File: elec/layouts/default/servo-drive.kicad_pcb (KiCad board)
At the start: 4 copper layers, 37.5 x 39 mm, 137 parts, among them U2 8Mhz

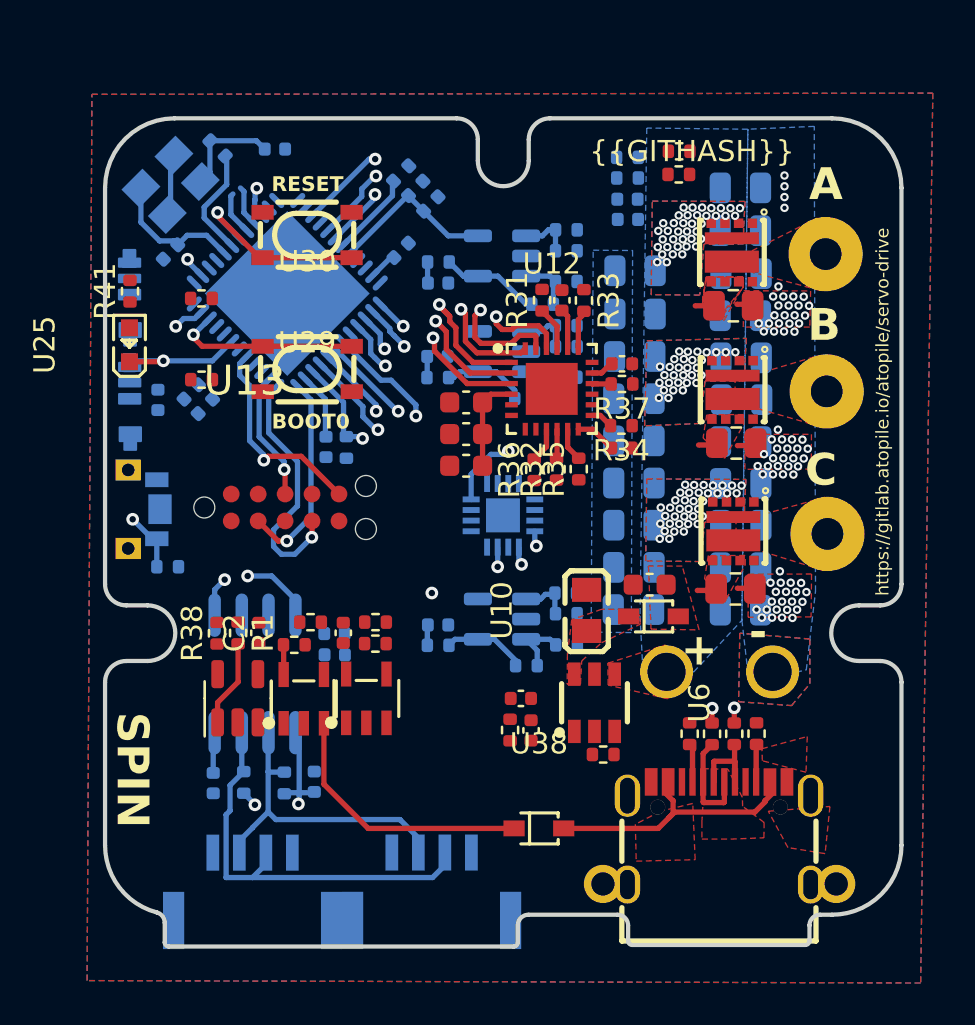
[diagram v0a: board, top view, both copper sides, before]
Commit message: big ol refactor, added lots of interfaces, changed pinout to match moteus controller, layout changed to add more connectors
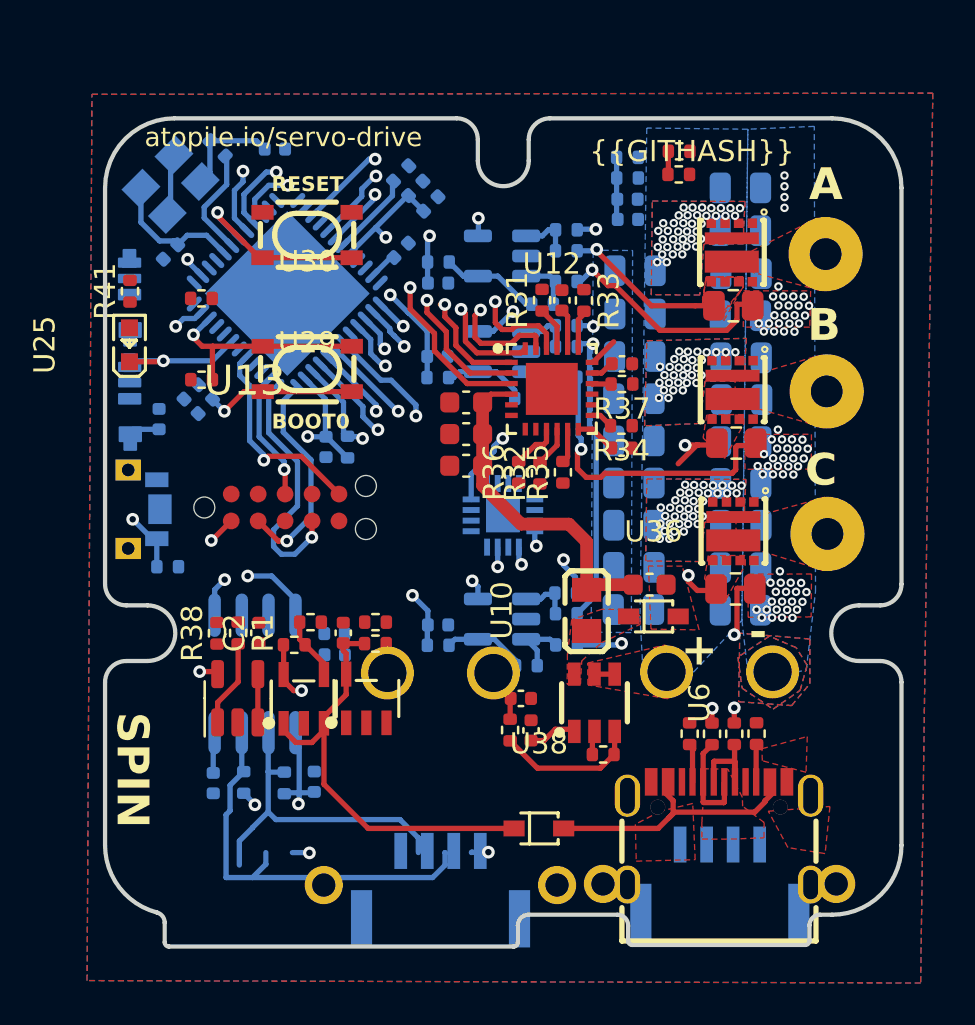
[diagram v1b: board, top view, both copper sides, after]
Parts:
- added U14: , lib:CONN-TH_XT30PW-M, B.Cu at (220.8, 112.8)
- moved U27 13.6 mm to (233.9, 118.0)
- moved U26 8.86 mm to (220.8, 118.3)
- moved C18 0.91 mm to (207.5, 95.8), turned to 90 degrees
- moved R32 0.80 mm to (225.5, 98.4)
- moved R35 0.76 mm to (226.5, 98.3)
- moved R36 0.74 mm to (224.5, 98.3)
- moved R15 0.06 mm to (216.4, 97.1)
- renumbered C44 to C42, C42 to C44
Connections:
- net SpinServoNEMA17-cs renamed SpinServoNEMA17-spi_cs
- net SpinServoNEMA17-enum_sw renamed SpinServoNEMA17-in
- net SpinServoNEMA17-mosi renamed SpinServoNEMA17-spi_mosi
- net SpinServoNEMA17-sck renamed SpinServoNEMA17-spi_sck
- net _a-high_gate-1 renamed _a-high_gate-2
- net _a-low_gate-1 renamed _a-low_gate-2
- net _b-high_gate-1 renamed _b-high_gate-2
- net _b-i_in renamed _b-gnd-1
- net _b-low_gate-1 renamed _b-low_gate-2
- net _c-gnd renamed _c-gnd-1
- net _c-high_gate-1 renamed _c-high_gate-2
- net _c-low_gate-1 renamed _c-low_gate-2
- net _hb-vcc_pwr renamed _hb-vcc_pwr-7
- net _hb-vcc_pwr-1 renamed _hb-vcc_pwr-9
- net _hb-vcc_pwr-2 renamed _hb-vcc_pwr-8
- net _i_sense-in-3 renamed _i_sense-in-5
- net _i_sense-in_n-3 renamed _i_sense-in_n-5
- net _i_sense-in_p-1 renamed _i_sense-output-9
- net _i_sense-in_p-2 renamed _i_sense-output-8
- net _i_sense-input-6 renamed _i_sense-p1-8
- net _i_sense-out-1 renamed _i_sense-in-6
- net _i_sense-output-4 renamed _i_sense-output-7
- net _i_sense-output-5 renamed _i_sense-in_n-6
- net _i_sense-p1-3 renamed _i_sense-p1-7
- net _i_sense-p1-4 renamed _i_sense-input-10
- net _i_sense-p1-5 renamed _i_sense-input-8
- net drv8300-EP-1 renamed drv8300-EP-2
- net drv8300-MODE-1 renamed drv8300-MODE-2
- net drv8300-NC1-1 renamed drv8300-NC1-2
- net drv8300-NC2-1 renamed drv8300-NC2-2
- net gate_reg-sw-1 renamed gate_reg-sw
- net micro_kit-in-1 renamed micro_kit-PB8_BOOT0
- net power_stage-DT renamed power_stage-DT-1
- net power_stage-GHA renamed power_stage-GHA-1
- net power_stage-GHB renamed power_stage-GHB-1
- net power_stage-GHC renamed power_stage-GHC-1
- net power_stage-GLA renamed power_stage-GLA-1
- net power_stage-GLB renamed power_stage-GLB-1
- net power_stage-GLC renamed power_stage-GLC-1
- net power_stage-bs renamed power_stage-bs-3
- net power_stage-bs-1 renamed power_stage-BSTC-1
- net power_stage-i_fb_zero renamed power_stage-i_fb_zero-1
- net vref_1V65-vref_unbuf-1 renamed vref_1V65-vref_unbuf-2
- C10 pad 1: _a-out -> SpinServoNEMA17-a_isense
- C11 pad 1: _b-out-1 -> SpinServoNEMA17-b_isense
- C12 pad 1: _c-i_fb -> SpinServoNEMA17-c_isense
- C14 pad 1: micro_kit-in-3 -> micro_kit-in-4
- R11 pad 2: micro_kit-in-2 -> micro_kit-in-3
- R13 pad 1: _i_sense-p1-2 -> _i_sense-input-7
- R16 pad 2: _a-out -> SpinServoNEMA17-a_isense
- R46 pad 2: _b-out-1 -> SpinServoNEMA17-b_isense
- R50 pad 1: _i_sense-input-7 -> _i_sense-input-9
- R52 pad 2: _c-i_fb -> SpinServoNEMA17-c_isense
- U15 pad 5: micro_kit-in-3 -> micro_kit-in-4
- U15 pad 7: micro_kit-in-2 -> micro_kit-in-3
- U17 pad 1: _i_sense-p1-2 -> _i_sense-input-7
- U2 pad 1: micro_kit-in-3 -> micro_kit-in-4
- U29 pad 1: micro_kit-in-2 -> micro_kit-in-3
- U29 pad 2: micro_kit-in-2 -> micro_kit-in-3
- U34 pad 1: _i_sense-input-7 -> _i_sense-input-9
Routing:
- net power_stage-i_fb_zero-1: track 0.00 -> 23.7 mm, vias 0 -> 2
- net SpinServoNEMA17-v_3: track 13.8 -> 30.0 mm, vias 0 -> 11
- net SpinServoNEMA17-a_isense: track 2.07 -> 17.7 mm, vias 0 -> 2
- net SpinServoNEMA17-b_isense: track 1.92 -> 17.0 mm, vias 0 -> 2
- net _i_sense-p1-8: track 0.00 -> 13.4 mm, vias 0 -> 1
- net SpinServoNEMA17-v_gate: track 4.51 -> 17.0 mm
- net _i_sense-input-8: track 0.00 -> 10.4 mm, vias 0 -> 2
- net _i_sense-input-10: track 0.00 -> 10.2 mm, vias 0 -> 2
- net _i_sense-p1-7: track 0.00 -> 9.89 mm, vias 0 -> 1
- net SpinServoNEMA17-v_5: track 12.7 -> 22.5 mm
- net micro_kit-in-2: track 8.93 -> 0.00 mm, vias 1 -> 0
- net _i_sense-input-9: track 0.00 -> 8.91 mm, vias 0 -> 2
- net gate_reg-fb-1: track 0.00 -> 6.80 mm
- net _i_sense-input-7: track 0.00 -> 6.75 mm, vias 0 -> 1
- net micro_kit-in-4: track 0.00 -> 6.51 mm
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- added copper zone on In2.Cu, net ldo_3v3-output
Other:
- board text added: "atopile.io/servo-drive"
- board text removed: "https://gitlab.atopile.io/atopile/servo-drive"

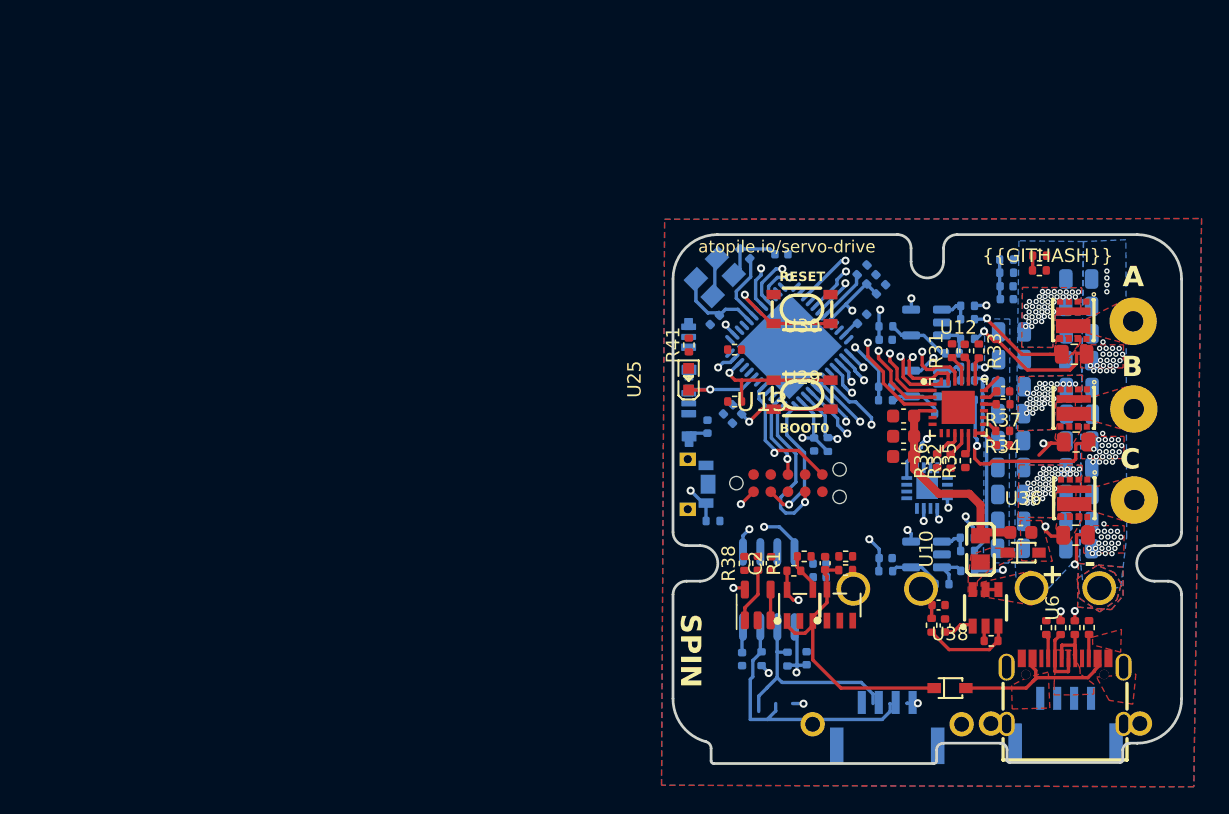
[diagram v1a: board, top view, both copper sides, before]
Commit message: Modified micro pinout to match moteus, because they are pretty sick, updated modules to use interfaces where posible, generated netlist and imported to Kicad project
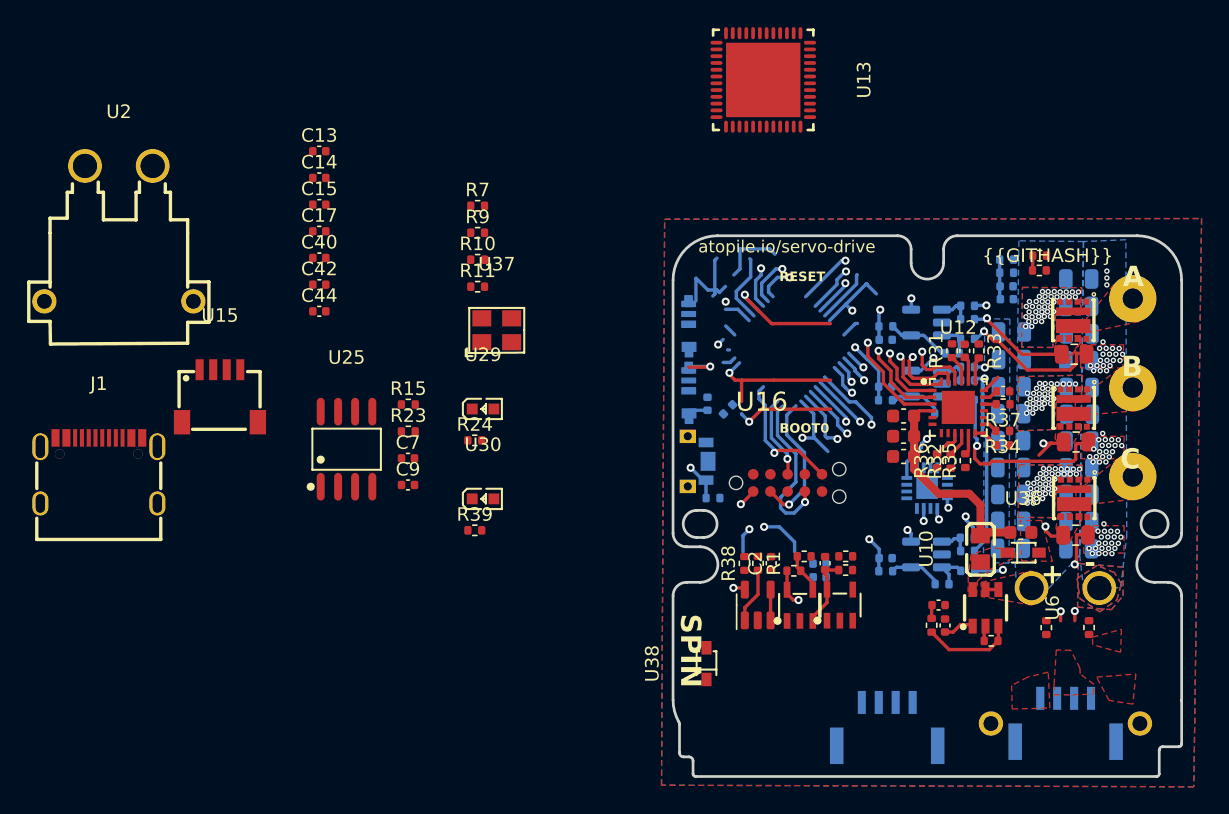
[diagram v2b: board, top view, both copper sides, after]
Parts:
- removed the C3 at (218.9, 87.9)
- removed the C4 at (219.6, 84.9)
- removed the C6 at (209.7, 95.2)
- removed R40: 60R, Resistor_SMD:R_0402_1005Metric
- removed R41: 1k, Resistor_SMD:R_0402_1005Metric
- removed the U14 at (220.8, 112.8)
- added C40: 1uF, Capacitor_SMD:C_0402_1005Metric, F.Cu at (178.8, 83.4)
- added C42: 20pF, Capacitor_SMD:C_0402_1005Metric, F.Cu at (178.8, 85.3)
- added C44: 20pF, Capacitor_SMD:C_0402_1005Metric, F.Cu at (178.8, 87.3)
- added U37: 8Mhz, lib:OSC-SMD_4P-L3.2-W2.5-BL, F.Cu at (191.9, 88.7)
- C13, C7, R7: moved to F.Cu
- C14, C15: value 20pF -> 100nF; moved to F.Cu
- C17: value 10nF -> 100nF; moved to F.Cu
- C9: value 1uF -> 10nF; moved to F.Cu
- R11: value 10k -> 1k5
- R15: value 1k5 -> 60R; moved to F.Cu
- R23: value 100k -> 60R
- R24: value 100k -> 1k; moved to F.Cu
- R39: value 60R -> 1k; moved to F.Cu
- U13: footprint lib:TAG-CONNECT_TC2050-IDC -> lib:UFQFPN-48_L7.0-W7.0-P0.50-BL-EP
- U15: footprint lib:UFQFPN-48_L7.0-W7.0-P0.50-BL-EP -> lib:CONN-SMD_4P-P1.00_SM04B-SRSS-TB-LF-SN; moved to F.Cu
- U16: footprint lib:SOIC-8_L4.9-W3.9-P1.27-LS6.0-BL -> lib:TAG-CONNECT_TC2050-IDC; moved to F.Cu
- U2: value 8Mhz -> (none); footprint lib:OSC-SMD_4P-L3.2-W2.5-BL -> lib:CONN-TH_XT30PW-M; moved to F.Cu
- U25: footprint lib:LED0603-RD -> lib:SOIC-8_L4.9-W3.9-P1.27-LS6.0-BL
- U29, U30: footprint lib:KEY-SMD_4P-L4.2-W3.2-P2.20-LS4.6 -> lib:LED0603-RD
- moved J1 73.2 mm to (162.6, 99.1)
- moved R9 52.9 mm to (190.5, 81.5), turned to 0 degrees
- moved R10 50.9 mm to (190.5, 83.5), turned to 0 degrees
- moved C13 48.8 mm to (178.8, 75.5), turned to 0 degrees
- moved C17 47.8 mm to (178.8, 81.4), turned to 0 degrees
- moved U2 44.1 mm to (164.0, 81.6), turned to 0 degrees
- moved U15 42.2 mm to (171.5, 93.5), turned to 0 degrees
- moved C7 37.1 mm to (185.4, 98.1), turned to 0 degrees
- moved C15 34.3 mm to (178.8, 79.4)
- moved R24 31.2 mm to (190.3, 96.8), turned to 0 degrees
- moved R15 31.1 mm to (185.4, 94.2), turned to 0 degrees
- moved C14 31.0 mm to (178.8, 77.4), turned to 0 degrees
- moved C9 30.1 mm to (185.4, 100.1), turned to 0 degrees
- moved U13 29.8 mm to (211.6, 70.2), turned to -90 degrees
- moved U25 25.8 mm to (180.8, 97.5), turned to 0 degrees
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- renumbered C40 to C3, C44 to C4, C42 to C6
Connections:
- net SpinServoNEMA17-anode renamed SpinServoNEMA17-vbus
- net SpinServoNEMA17-data_in renamed SpinServoNEMA17-data_out
- net _a-gnd-1 renamed _a-i_in-1
- net _b-gnd-1 renamed _b-i_in-1
- net _c-gnd-1 renamed _c-i_in-1
- net _i_sense-in-5 renamed _i_sense-out-4
- net _i_sense-in_n-5 renamed _i_sense-in_n-7
- net _i_sense-input-8 renamed _i_sense-input-11
- net _i_sense-output-8 renamed _i_sense-in_p-1
- net _i_sense-output-9 renamed _i_sense-in_p-2
- net _i_sense-p1-8 renamed _i_sense-input-12
- net gate_reg-sw renamed gate_reg-sw-1
- net ldo_3v3-output renamed ldo_3v3-adj-1
- net usb-sbu-1 renamed usbc-sbu-1
- C1 pad 1: SpinServoNEMA17-v_3 -> SpinServoNEMA17-vcc
- C13 pad 1: SpinServoNEMA17-v_3 -> SpinServoNEMA17-vcc
- C14 pad 1: micro_kit-in-4 -> SpinServoNEMA17-vcc
- C15 pad 1: micro_kit-out-1 -> SpinServoNEMA17-vcc
- C16 pad 1: SpinServoNEMA17-v_5 -> SpinServoNEMA17-gnd
- C17 pad 1: canbus-v_mid-2 -> SpinServoNEMA17-vcc
- C18 pad 1: SpinServoNEMA17-v_5 -> SpinServoNEMA17-gnd
- C19 pad 1: SpinServoNEMA17-v_3 -> SpinServoNEMA17-vcc
- C20 pad 1: SpinServoNEMA17-v_pwr -> power_stage-vcc_pwr-1
- C21 pad 1: SpinServoNEMA17-v_pwr -> power_stage-vcc_pwr-1
- C22 pad 1: SpinServoNEMA17-v_pwr -> power_stage-vcc_pwr-1
- C23 pad 1: SpinServoNEMA17-v_gate -> SpinServoNEMA17-gnd
- C25 pad 1: SpinServoNEMA17-v_pwr -> power_stage-vcc_pwr-1
- C26 pad 1: SpinServoNEMA17-v_pwr -> power_stage-vcc_pwr-1
- C27 pad 1: SpinServoNEMA17-v_pwr -> power_stage-vcc_pwr-1
- C28 pad 1: SpinServoNEMA17-v_pwr -> SpinServoNEMA17-vcc-1
- C29 pad 1: SpinServoNEMA17-v_pwr -> power_stage-vcc_pwr-1
- C3 pad 1: SpinServoNEMA17-v_pwr -> power_stage-vcc_pwr-1
- C30 pad 1: SpinServoNEMA17-v_pwr -> power_stage-vcc_pwr-1
- C31 pad 1: SpinServoNEMA17-v_gate -> SpinServoNEMA17-gnd
- C32 pad 1: SpinServoNEMA17-v_gate -> SpinServoNEMA17-gnd
- C33 pad 1: SpinServoNEMA17-out -> SpinServoNEMA17-vin_sense
- C34 pad 1: SpinServoNEMA17-out -> SpinServoNEMA17-vin_sense
- C35 pad 1: SpinServoNEMA17-v_pwr -> power_stage-vcc_pwr-1
- C36 pad 1: SpinServoNEMA17-v_pwr -> power_stage-vcc_pwr-1
- C37 pad 1: SpinServoNEMA17-v_pwr -> power_stage-vcc_pwr-1
- C38 pad 1: SpinServoNEMA17-v_pwr -> power_stage-vcc_pwr-1
- C39 pad 1: SpinServoNEMA17-v_pwr -> power_stage-vcc_pwr-1
- C4 pad 1: SpinServoNEMA17-v_pwr -> power_stage-vcc_pwr-1
- C41 pad 1: power_stage-bs-3 -> power_stage-bs-4
- C43 pad 1: power_stage-bs-2 -> power_stage-bs-3
- C45 pad 1: power_stage-BSTC-1 -> power_stage-bs-2
- C46 pad 1: SpinServoNEMA17-v_3 -> SpinServoNEMA17-vcc
- C47 pad 1: SpinServoNEMA17-v_pwr -> power_stage-vcc_pwr-1
- C48 pad 1: SpinServoNEMA17-v_pwr -> power_stage-vcc_pwr-1
- C49 pad 1: SpinServoNEMA17-v_pwr -> power_stage-vcc_pwr-1
- C5 pad 1: SpinServoNEMA17-v_gate -> SpinServoNEMA17-gnd
- C6 pad 1: SpinServoNEMA17-v_pwr -> power_stage-vcc_pwr-1
- C7 pad 1: SpinServoNEMA17-v_3 -> canbus-v_3_3-2
- C7 pad 2: SpinServoNEMA17-gnd -> canbus-gnd-2
- C8 pad 1: SpinServoNEMA17-v_gate -> SpinServoNEMA17-gnd
- C9 pad 1: SpinServoNEMA17-v_3 -> canbus-v_mid-2
- C9 pad 2: SpinServoNEMA17-gnd -> canbus-gnd-2
- J1 pad A7: SpinServoNEMA17-dm -> SpinServoNEMA17-gnd
- J1 pad B7: SpinServoNEMA17-dm -> SpinServoNEMA17-gnd
- R1 pad 1: SpinServoNEMA17-v_3 -> SpinServoNEMA17-vcc
- R10 pad 1: micro_kit-PA11-1 -> SpinServoNEMA17-dp
- R10 pad 2: SpinServoNEMA17-dm -> SpinServoNEMA17-dp
- R11 pad 1: SpinServoNEMA17-v_3 -> SpinServoNEMA17-gnd
- R11 pad 2: micro_kit-in-3 -> SpinServoNEMA17-vcc
- R12 pad 1: _i_sense-in_n-4 -> _i_sense-in_n-6
- R12 pad 2: _i_sense-in-4 -> _i_sense-out-3
- R13 pad 1: _i_sense-input-7 -> _i_sense-input-9
- R15 pad 1: micro_kit-PA12-1 -> SpinServoNEMA17-p3
- R15 pad 2: SpinServoNEMA17-v_3 -> canbus-v_mid-2
- R16 pad 1: _i_sense-in-4 -> _i_sense-out-3
- R17 pad 1: SpinServoNEMA17-v_5 -> SpinServoNEMA17-gnd
- R2 pad 1: SpinServoNEMA17-v_3 -> SpinServoNEMA17-vcc
- R21 pad 1: SpinServoNEMA17-v_3 -> SpinServoNEMA17-vcc
- R23 pad 1: micro_kit-PB8_BOOT0 -> SpinServoNEMA17-p2
- R23 pad 2: SpinServoNEMA17-gnd -> canbus-v_mid-2
- R24 pad 1: micro_kit-PB2-1 -> debug_led_1-A-2
- R27 pad 1: SpinServoNEMA17-v_pwr -> SpinServoNEMA17-vcc-1
- R27 pad 2: SpinServoNEMA17-out -> SpinServoNEMA17-vin_sense
- R28 pad 1: SpinServoNEMA17-out -> SpinServoNEMA17-vin_sense
- R29 pad 1: SpinServoNEMA17-v_gate -> SpinServoNEMA17-gnd
- R39 pad 1: SpinServoNEMA17-p2 -> debug_led_2-A-2
- R39 pad 2: canbus-v_mid-2 -> SpinServoNEMA17-gnd
- R48 pad 1: _i_sense-input-10 -> _i_sense-input-14
- R48 pad 2: _i_sense-in_n-6 -> _i_sense-in_n-8
- R49 pad 1: _i_sense-in_n-6 -> _i_sense-in_n-8
- R49 pad 2: _i_sense-in-6 -> _i_sense-in-4
- R50 pad 1: _i_sense-input-9 -> _i_sense-input-13
- R52 pad 1: _i_sense-in-6 -> _i_sense-in-4
- R6 pad 1: _i_sense-p1-7 -> _i_sense-input-10
- R6 pad 2: _i_sense-in_n-4 -> _i_sense-in_n-6
- R7 pad 1: micro_kit-PF1_OSC_OUT-1 -> micro-input-2
- R7 pad 2: micro_kit-out-1 -> micro-out-1
- R9 pad 1: micro_kit-PA12-1 -> SpinServoNEMA17-gnd
- R9 pad 2: SpinServoNEMA17-dp -> SpinServoNEMA17-gnd
- U10 pad 2: SpinServoNEMA17-v_gate -> SpinServoNEMA17-gnd
- U11 pad 2: SpinServoNEMA17-v_3 -> SpinServoNEMA17-vcc
- U12 pad 1: SpinServoNEMA17-ctrl_a_low -> SpinServoNEMA17-phase_a
- U12 pad 14: power_stage-BSTC-1 -> power_stage-bs-2
- U12 pad 17: power_stage-bs-2 -> power_stage-bs-3
- U12 pad 2: SpinServoNEMA17-ctrl_b_low -> SpinServoNEMA17-phase_b
- U12 pad 20: power_stage-bs-3 -> power_stage-bs-4
- U12 pad 22: SpinServoNEMA17-ctrl_a_high -> SpinServoNEMA17-phase_a
- U12 pad 23: SpinServoNEMA17-ctrl_b_high -> SpinServoNEMA17-phase_b
- U12 pad 24: SpinServoNEMA17-ctrl_c_high -> SpinServoNEMA17-phase_c
- U12 pad 25: drv8300-EP-2 -> SpinServoNEMA17-gnd
- U12 pad 3: SpinServoNEMA17-ctrl_c_low -> SpinServoNEMA17-phase_c
- U12 pad 4: SpinServoNEMA17-v_gate -> SpinServoNEMA17-gnd
- U12 pad 5: drv8300-MODE-2 -> SpinServoNEMA17-vcc
- U13 pad 1: SpinServoNEMA17-v_3 -> micro-VBAT-2
- U13 pad 10: jtag-rst-2 -> SpinServoNEMA17-phase_c
- U13 pad 2: micro_kit-tms-1 -> micro-PC13-2
- U13 pad 3: SpinServoNEMA17-gnd -> micro-PC14_OSC32_IN-2
- U13 pad 4: micro_kit-tck-1 -> micro-PC15_OSC32_OUT-2
- U13 pad 5: SpinServoNEMA17-gnd -> micro-PF0_OSC_IN
- U13 pad 6: micro_kit-tdo-1 -> micro-input-2
- U13 pad 7: (no net) -> micro-PG10_NRST-2
- U13 pad 8: micro_kit-tdi-1 -> SpinServoNEMA17-phase_a
- U13 pad 9: (no net) -> SpinServoNEMA17-phase_b
- U14 pad 2: SpinServoNEMA17-v_pwr -> SpinServoNEMA17-vcc-1
- U15 pad 1: micro-VBAT-2 -> SpinServoNEMA17-gnd
- U15 pad 2: SpinServoNEMA17-in -> SpinServoNEMA17-vcc
- U15 pad 3: micro-PC14_OSC32_IN-2 -> SpinServoNEMA17-sda
- U15 pad 4: micro-PC15_OSC32_OUT-2 -> SpinServoNEMA17-gnd
- U15 pad 5: micro_kit-in-4 -> (no net)
- U15 pad 6: micro_kit-PF1_OSC_OUT-1 -> (no net)
- U16 pad 1: micro_kit-can_tx-1 -> SpinServoNEMA17-vcc
- U16 pad 2: SpinServoNEMA17-gnd -> micro-tms
- U16 pad 3: SpinServoNEMA17-v_3 -> SpinServoNEMA17-gnd
- U16 pad 4: micro_kit-PB8_BOOT0 -> micro-tck-1
- U16 pad 5: canbus-v_mid-2 -> SpinServoNEMA17-gnd
- U16 pad 6: SpinServoNEMA17-p3 -> micro-PB3
- U16 pad 7: SpinServoNEMA17-p2 -> (no net)
- U16 pad 8: SpinServoNEMA17-gnd -> micro-PA15
- U17 pad 1: _i_sense-input-7 -> _i_sense-input-9
- U18 pad 12: SpinServoNEMA17-spi_sck -> SpinServoNEMA17-sck
- U18 pad 13: SpinServoNEMA17-v_3 -> SpinServoNEMA17-vcc
- U18 pad 4: SpinServoNEMA17-spi_mosi -> SpinServoNEMA17-mosi
- U18 pad 5: SpinServoNEMA17-spi_cs -> SpinServoNEMA17-cs
- U18 pad 7: SpinServoNEMA17-spi_miso -> SpinServoNEMA17-miso
- U19 pad 1: _i_sense-p1-7 -> _i_sense-input-10
- U2 pad 1: micro_kit-in-4 -> xt30_2-gnd-1
- U2 pad 2: SpinServoNEMA17-gnd -> xt30_2-vin-1
- U2 pad 3: micro_kit-out-1 -> (no net)
- U2 pad 4: SpinServoNEMA17-gnd -> (no net)
- U20 pad 3: _i_sense-in_n-4 -> _i_sense-in_n-6
- U20 pad 4: _i_sense-in-4 -> _i_sense-out-3
- U20 pad 5: SpinServoNEMA17-v_3 -> SpinServoNEMA17-vcc
- U21 pad 5: SpinServoNEMA17-v_3 -> SpinServoNEMA17-vcc
- U22 pad 1: SpinServoNEMA17-v_gate -> SpinServoNEMA17-gnd
- U22 pad 3: SpinServoNEMA17-v_gate -> SpinServoNEMA17-gnd
- U22 pad 5: SpinServoNEMA17-v_5 -> SpinServoNEMA17-gnd
- U23 pad 1: SpinServoNEMA17-v_5 -> SpinServoNEMA17-gnd
- U23 pad 3: SpinServoNEMA17-v_5 -> SpinServoNEMA17-gnd
- U23 pad 5: SpinServoNEMA17-v_3 -> SpinServoNEMA17-vcc
- U24 pad 3: _i_sense-in_n-6 -> _i_sense-in_n-8
- U24 pad 4: _i_sense-in-6 -> _i_sense-in-4
- U24 pad 5: SpinServoNEMA17-v_3 -> SpinServoNEMA17-vcc
- U25 pad 1: SpinServoNEMA17-led_pixel -> SpinServoNEMA17-gnd
- U25 pad 2: indicator-A-1 -> canbus-gnd-2
- U26 pad 1: SpinServoNEMA17-v_3 -> SpinServoNEMA17-gnd
- U27 pad 1: SpinServoNEMA17-v_3 -> SpinServoNEMA17-gnd
- U27 pad 2: SpinServoNEMA17-p2 -> SpinServoNEMA17-p3
- U27 pad 3: SpinServoNEMA17-p3 -> SpinServoNEMA17-p2
- U29 pad 1: micro_kit-in-3 -> micro-PF0_OSC_IN
- U29 pad 2: micro_kit-in-3 -> debug_led_1-A-2
- U30 pad 1: micro_kit-PB8_BOOT0 -> micro-input-2
- U30 pad 2: micro_kit-PB8_BOOT0 -> debug_led_2-A-2
- U32 pad 1: SpinServoNEMA17-v_5 -> SpinServoNEMA17-gnd
- U34 pad 1: _i_sense-input-9 -> _i_sense-input-13
- U35 pad 1: _i_sense-input-10 -> _i_sense-input-14
- U38 pad 1: SpinServoNEMA17-v_5 -> SpinServoNEMA17-gnd
- U4 pad 5: SpinServoNEMA17-v_3 -> SpinServoNEMA17-vcc
- U5 pad 1: SpinServoNEMA17-v_5 -> SpinServoNEMA17-gnd
- U6 pad 4: SpinServoNEMA17-v_pwr -> SpinServoNEMA17-vcc-1
- U6 pad 5: SpinServoNEMA17-v_pwr -> SpinServoNEMA17-vcc-1
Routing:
- net (no net): track 0.00 -> 153.2 mm, vias 0 -> 12
- net SpinServoNEMA17-phase_a: track 0.00 -> 34.3 mm, vias 0 -> 4
- net SpinServoNEMA17-phase_b: track 0.00 -> 32.6 mm, vias 0 -> 4
- net micro_kit-PA12-1: track 31.7 -> 0.00 mm, vias 2 -> 0
- net SpinServoNEMA17-phase_c: track 0.00 -> 31.3 mm, vias 0 -> 4
- net micro_kit-PA11-1: track 30.1 -> 0.00 mm, vias 2 -> 0
- net SpinServoNEMA17-v_3: track 30.0 -> 0.00 mm, vias 11 -> 0
- net micro_kit-PB8_BOOT0: track 26.8 -> 0.00 mm, vias 2 -> 0
- net SpinServoNEMA17-v_5: track 22.5 -> 0.00 mm
- net SpinServoNEMA17-p2: track 19.8 -> 0.00 mm
- net SpinServoNEMA17-spi_mosi: track 19.0 -> 0.00 mm, vias 2 -> 0
- net SpinServoNEMA17-mosi: track 0.00 -> 19.0 mm, vias 0 -> 2
- net SpinServoNEMA17-gnd: track 5.98 -> 24.6 mm, vias 68 -> 62
- net SpinServoNEMA17-ctrl_a_low: track 17.6 -> 0.00 mm, vias 2 -> 0
- net SpinServoNEMA17-v_gate: track 17.0 -> 0.00 mm
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- added copper zone on F.Cu, net SpinServoNEMA17-vcc-1
- added copper zone on B.Cu, net power_stage-vcc_pwr-1
- added copper zone on F.Cu, net power_stage-vcc_pwr-1
- added copper zone on In2.Cu, net power_stage-vcc_pwr-1
- removed copper zone on B.Cu, net SpinServoNEMA17-v_pwr
- removed copper zone on F.Cu, net SpinServoNEMA17-v_pwr
- removed copper zone on In2.Cu, net SpinServoNEMA17-v_pwr
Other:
- board size 37.5 x 39 mm -> 37.6 x 39.9 mm
